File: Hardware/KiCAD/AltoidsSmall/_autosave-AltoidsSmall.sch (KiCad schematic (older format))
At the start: 8 parts, among them U1 SC662K-3.3V, U4 USB_B_micro, U6 SC662K-3.3V

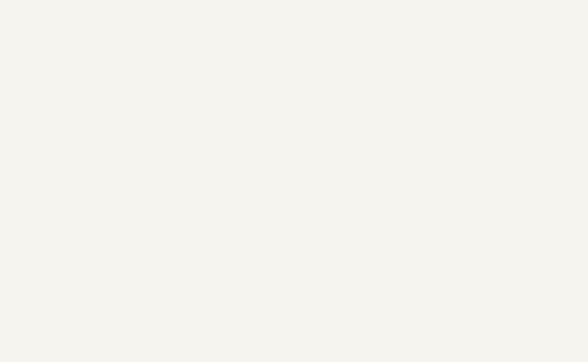
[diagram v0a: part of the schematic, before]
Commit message: Added bom
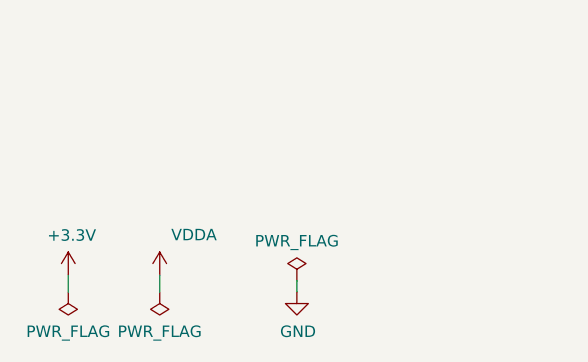
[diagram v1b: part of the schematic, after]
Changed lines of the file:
@@
 $EndComp
 Connection ~ 6200 1950
+$Comp
+L power:PWR_FLAG #FLG0101
+U 1 1 6013D1B8
+P 850 7425
+F 0 "#FLG0101" H 850 7500 50  0001 C CNN
+F 1 "PWR_FLAG" H 850 7598 50  0000 C CNN
+F 2 "" H 850 7425 50  0001 C CNN
+F 3 "~" H 850 7425 50  0001 C CNN
+	1    850  7425
+	-1   0    0    1
+$EndComp
+$Comp
+L power:PWR_FLAG #FLG0102
+U 1 1 6013DECB
+P 1250 7425
+F 0 "#FLG0102" H 1250 7500 50  0001 C CNN
+F 1 "PWR_FLAG" H 1250 7598 50  0000 C CNN
+F 2 "" H 1250 7425 50  0001 C CNN
+F 3 "~" H 1250 7425 50  0001 C CNN
+	1    1250 7425
+	-1   0    0    1
+$EndComp
+$Comp
+L AltoidsSmall:+3.3V #PWR0110
+U 1 1 601421D4
+P 850 7350
+F 0 "#PWR0110" H 850 7200 50  0001 C CNN
+F 1 "+3.3V" H 865 7523 50  0000 C CNN
+F 2 "" H 850 7350 50  0001 C CNN
+F 3 "" H 850 7350 50  0001 C CNN
+	1    850  7350
+	1    0    0    -1
+$EndComp
+$Comp
+L power:VDDA #PWR?
+U 1 1 60143A35
+P 1250 7350
+AR Path="/5FF2DABE/60143A35" Ref="#PWR?"  Part="1"
+AR Path="/60143A35" Ref="#PWR0111"  Part="1"
+F 0 "#PWR0111" H 1250 7200 50  0001 C CNN
+F 1 "VDDA" H 1400 7525 50  0000 C CNN
+F 2 "" H 1250 7350 50  0001 C CNN
+F 3 "" H 1250 7350 50  0001 C CNN
+	1    1250 7350
+	1    0    0    -1
+$EndComp
+Wire Wire Line
+	850  7350 850  7425
+Wire Wire Line
+	1250 7350 1250 7425
+$Comp
+L power:PWR_FLAG #FLG0103
+U 1 1 6014A5D2
+P 1850 7375
+F 0 "#FLG0103" H 1850 7450 50  0001 C CNN
+F 1 "PWR_FLAG" H 1850 7548 50  0000 C CNN
+F 2 "" H 1850 7375 50  0001 C CNN
+F 3 "~" H 1850 7375 50  0001 C CNN
+	1    1850 7375
+	1    0    0    -1
+$EndComp
+$Comp
+L power:GND #PWR0112
+U 1 1 6014B19E
+P 1850 7425
+F 0 "#PWR0112" H 1850 7175 50  0001 C CNN
+F 1 "GND" H 1855 7252 50  0000 C CNN
+F 2 "" H 1850 7425 50  0001 C CNN
+F 3 "" H 1850 7425 50  0001 C CNN
+	1    1850 7425
+	1    0    0    -1
+$EndComp
+Wire Wire Line
+	1850 7375 1850 7425
 $EndSCHEMATC

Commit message: Added labels to pins, Added part numbers
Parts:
- C1, C16, C17, C2: Digikey (none) -> 1276-6524-1-ND
- U1, U6: Digikey (none) -> AP2210N-3.3TRG1DICT-ND
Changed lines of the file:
@@
 F 2 "Package_TO_SOT_SMD:SOT-23" H 5100 1950 50  0001 C CNN
 F 3 "" H 5100 1950 50  0001 C CNN
+F 4 "AP2210N-3.3TRG1DICT-ND" H 5100 1950 50  0001 C CNN "Digikey"
 	1    5100 1950
 	1    0    0    -1
@@
 F 2 "Capacitor_SMD:C_0603_1608Metric_Pad1.05x0.95mm_HandSolder" H 5600 2125 50  0001 C CNN
 F 3 "~" H 5600 2125 50  0001 C CNN
+F 4 "1276-6524-1-ND" H 5600 2125 50  0001 C CNN "Digikey"
 	1    5600 2125
 	1    0    0    -1
@@
 F 2 "Capacitor_SMD:C_0603_1608Metric_Pad1.05x0.95mm_HandSolder" H 4600 2100 50  0001 C CNN
 F 3 "~" H 4600 2100 50  0001 C CNN
+F 4 "1276-6524-1-ND" H 4600 2100 50  0001 C CNN "Digikey"
 	1    4600 2100
 	1    0    0    -1
@@
 F 2 "Package_TO_SOT_SMD:SOT-23" H 6700 1950 50  0001 C CNN
 F 3 "" H 6700 1950 50  0001 C CNN
+F 4 "AP2210N-3.3TRG1DICT-ND" H 6700 1950 50  0001 C CNN "Digikey"
 	1    6700 1950
 	1    0    0    -1
@@
 F 2 "Capacitor_SMD:C_0603_1608Metric_Pad1.05x0.95mm_HandSolder" H 6200 2125 50  0001 C CNN
 F 3 "~" H 6200 2125 50  0001 C CNN
+F 4 "1276-6524-1-ND" H 6200 2125 50  0001 C CNN "Digikey"
 	1    6200 2125
 	1    0    0    -1
@@
 F 2 "Capacitor_SMD:C_0603_1608Metric_Pad1.05x0.95mm_HandSolder" H 7275 2125 50  0001 C CNN
 F 3 "~" H 7275 2125 50  0001 C CNN
+F 4 "1276-6524-1-ND" H 7275 2125 50  0001 C CNN "Digikey"
 	1    7275 2125
 	1    0    0    -1
